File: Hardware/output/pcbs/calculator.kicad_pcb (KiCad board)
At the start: 4 copper layers, 70.5 x 143 mm, 46 parts

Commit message: feat: implement alpha key input support and unify error handling in RetroUIController
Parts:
- moved Disp 6.00 mm to (29.5, -125.9)
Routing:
- net P21: track 185.1 -> 51.6 mm, vias 3 -> 0
- net P20: track 89.1 -> 131.7 mm, vias 0 -> 3
- net P6: track 162.6 -> 197.1 mm, vias 4 -> 5
- net P1: track 134.6 -> 165.9 mm, vias 5 -> 4
- net P4: track 109.3 -> 132.8 mm, vias 6 -> 4
- net P10: track 173.3 -> 195.4 mm, vias 3 -> 4
- net P5: track 145.5 -> 167.1 mm, vias 3 -> 4
- net P14: track 135.2 -> 153.6 mm, vias 2 -> 1
- net P18: track 1.74 -> 19.9 mm
- net P16: track 86.2 -> 103.8 mm, vias 2 -> 1
- net GND: track 54.9 -> 67.0 mm, vias 1 -> 0
- net P0: track 129.8 -> 141.5 mm
- net P15: track 133.2 -> 142.1 mm, vias 2 -> 1
- net P9: track 141.7 -> 148.4 mm, vias 2 -> 1
- net P7: track 148.7 -> 155.3 mm, vias 2 -> 1
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- removed copper zone on In1.Cu, net GND
- removed copper zone on In2.Cu, net GND
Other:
- copper layers 4 -> 2

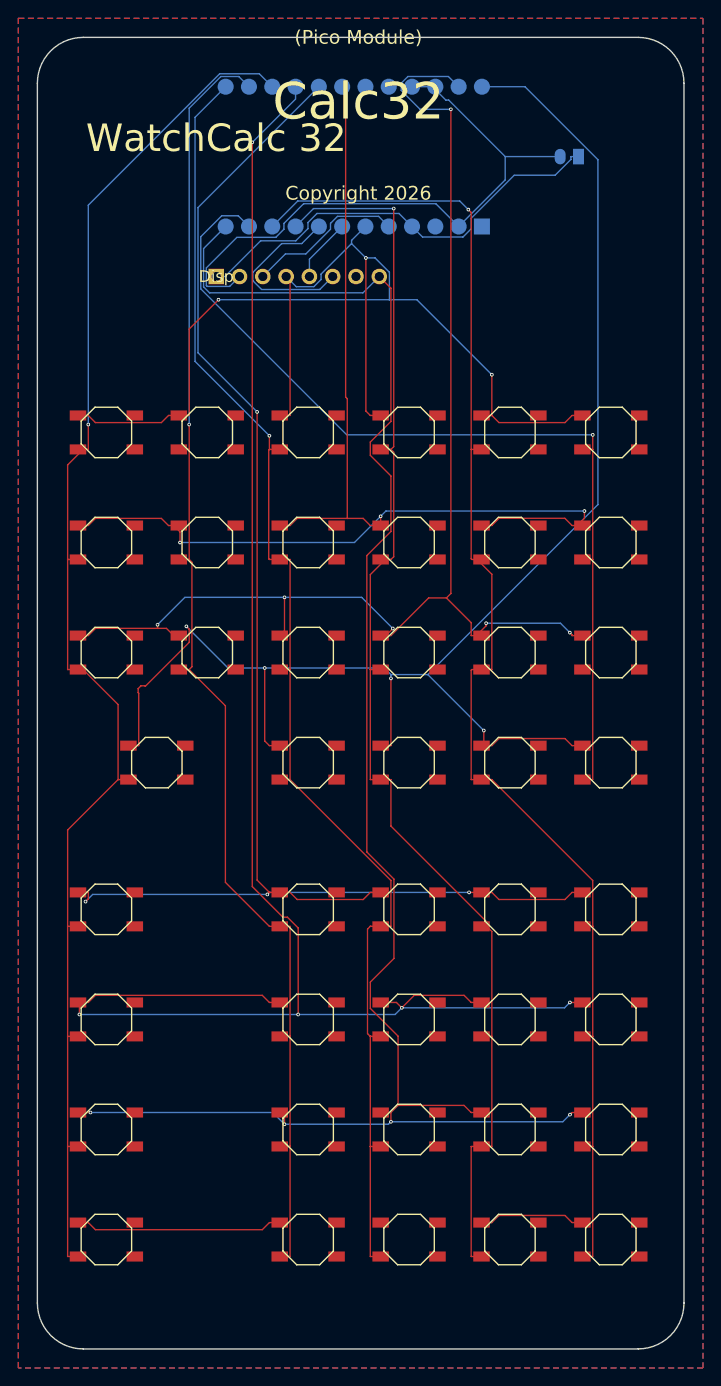
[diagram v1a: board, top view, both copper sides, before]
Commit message: fix: resolve display formatting bugs in hardware wrapper and streamline PCB manufacturing and ordering documentation.
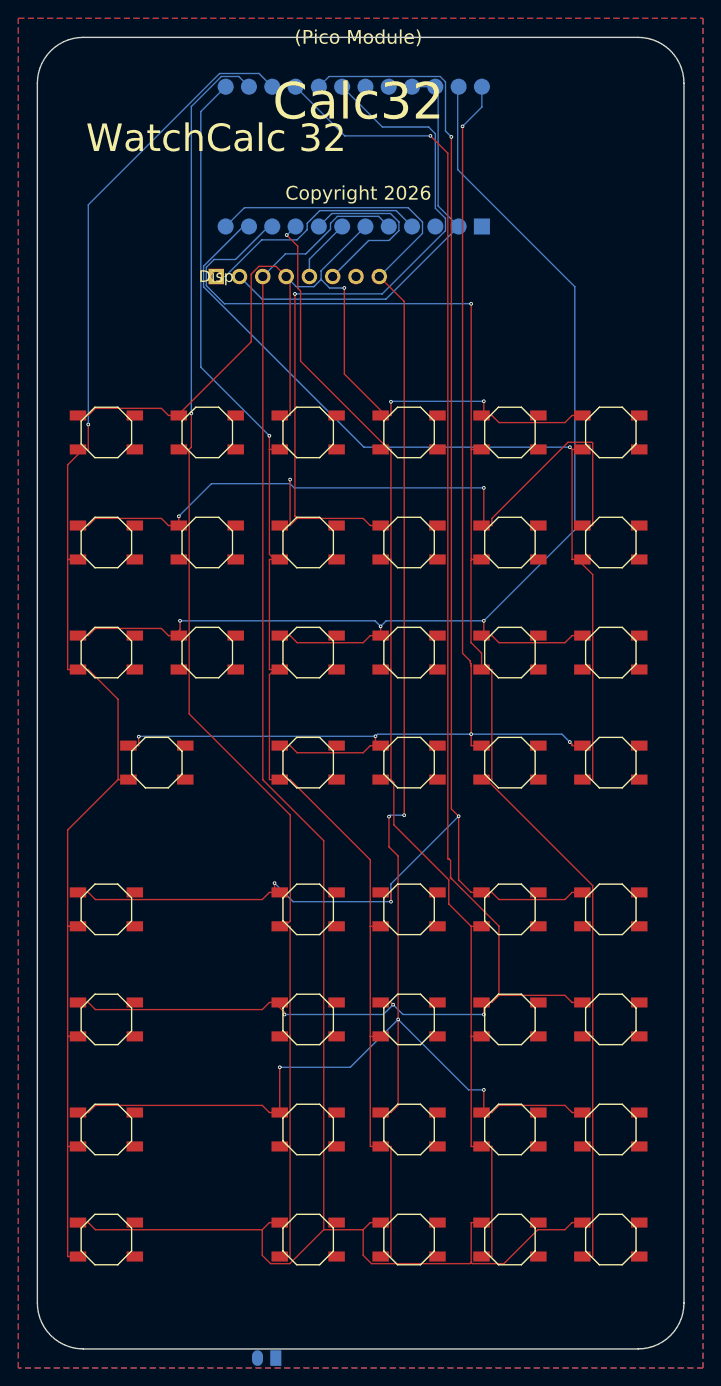
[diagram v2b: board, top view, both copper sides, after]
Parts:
- moved JST1 135.1 mm to (35.0, -8.00)
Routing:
- net P21: track 51.6 -> 199.0 mm
- net P4: track 132.8 -> 162.6 mm
- net P1: track 165.9 -> 138.1 mm, vias 4 -> 5
- net P20: track 131.7 -> 108.6 mm
- net VCC: track 48.4 -> 25.5 mm
- net P6: track 197.1 -> 175.4 mm, vias 5 -> 4
- net GND: track 67.0 -> 47.0 mm
- net P15: track 142.1 -> 131.0 mm
- net P16: track 103.8 -> 97.7 mm
- net P14: track 153.6 -> 158.9 mm
- net P5: track 167.1 -> 168.5 mm
- net P9: track 148.4 -> 147.1 mm
- net P0: track 141.5 -> 140.9 mm, vias 6 -> 3
- net P10: track 195.4 -> 195.9 mm, vias 4 -> 5

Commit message: feat: update PCB layout and chassis assets, and refine calculator engine logic
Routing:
- net P21: track 199.0 -> 614.0 mm, vias 0 -> 2
- net P6: track 175.4 -> 587.2 mm, vias 4 -> 13
- net P10: track 195.9 -> 599.6 mm, vias 5 -> 19
- net P8: track 146.4 -> 484.5 mm, vias 1 -> 3
- net P7: track 155.7 -> 463.0 mm, vias 1 -> 3
- net P5: track 168.5 -> 475.2 mm, vias 4 -> 13
- net P9: track 147.1 -> 451.6 mm, vias 1 -> 3
- net P15: track 131.0 -> 430.9 mm, vias 1 -> 3
- net P14: track 158.9 -> 454.9 mm, vias 1 -> 3
- net P0: track 140.9 -> 434.3 mm, vias 3 -> 10
- net P1: track 138.1 -> 409.5 mm, vias 5 -> 12
- net P4: track 162.6 -> 373.4 mm, vias 4 -> 12
- net P20: track 108.6 -> 300.7 mm
- net P16: track 97.7 -> 288.2 mm, vias 1 -> 3
- net GND: track 47.0 -> 147.3 mm
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- added copper zone on B.Cu, net (none)
- added copper zone on F.Cu, net (none)
- removed copper zone on B.Cu, net GND
- removed copper zone on F.Cu, net GND

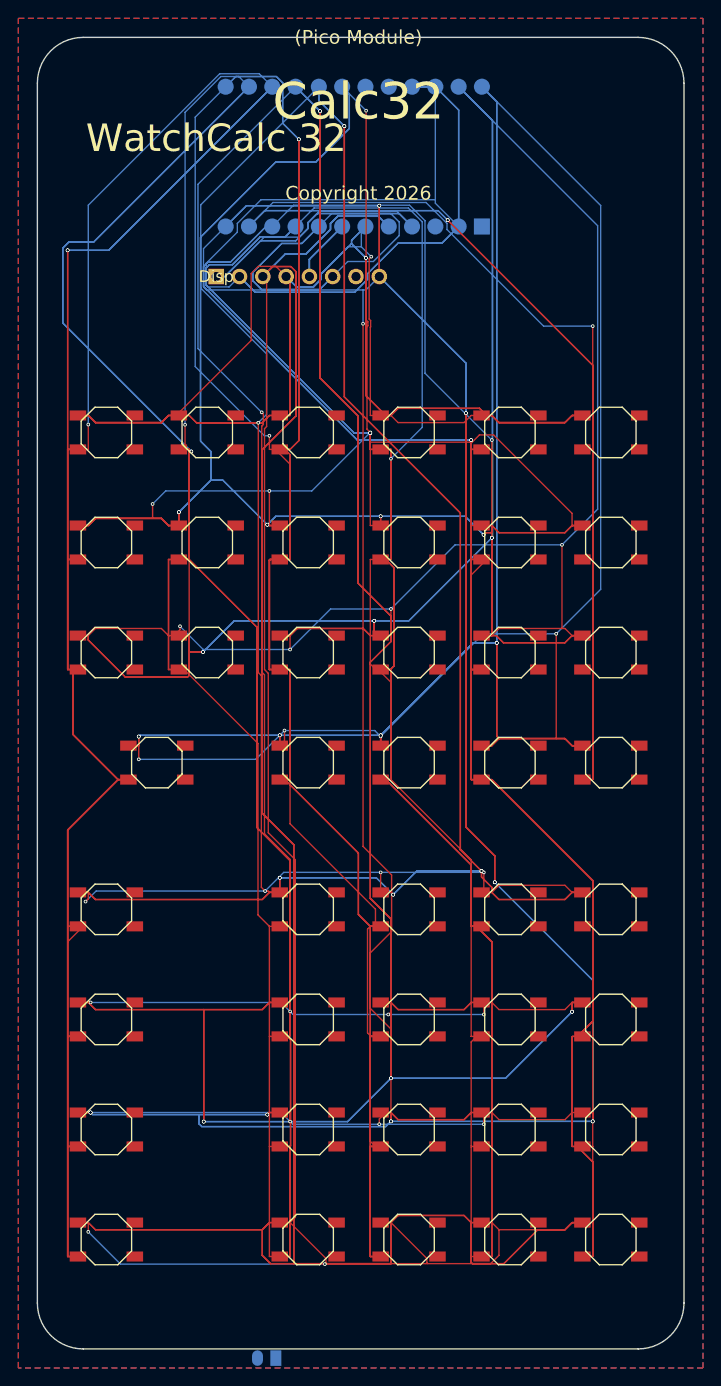
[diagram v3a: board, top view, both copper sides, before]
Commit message: refactor: update stack lift logic, add STL batching script, and adjust hardware geometry/routing
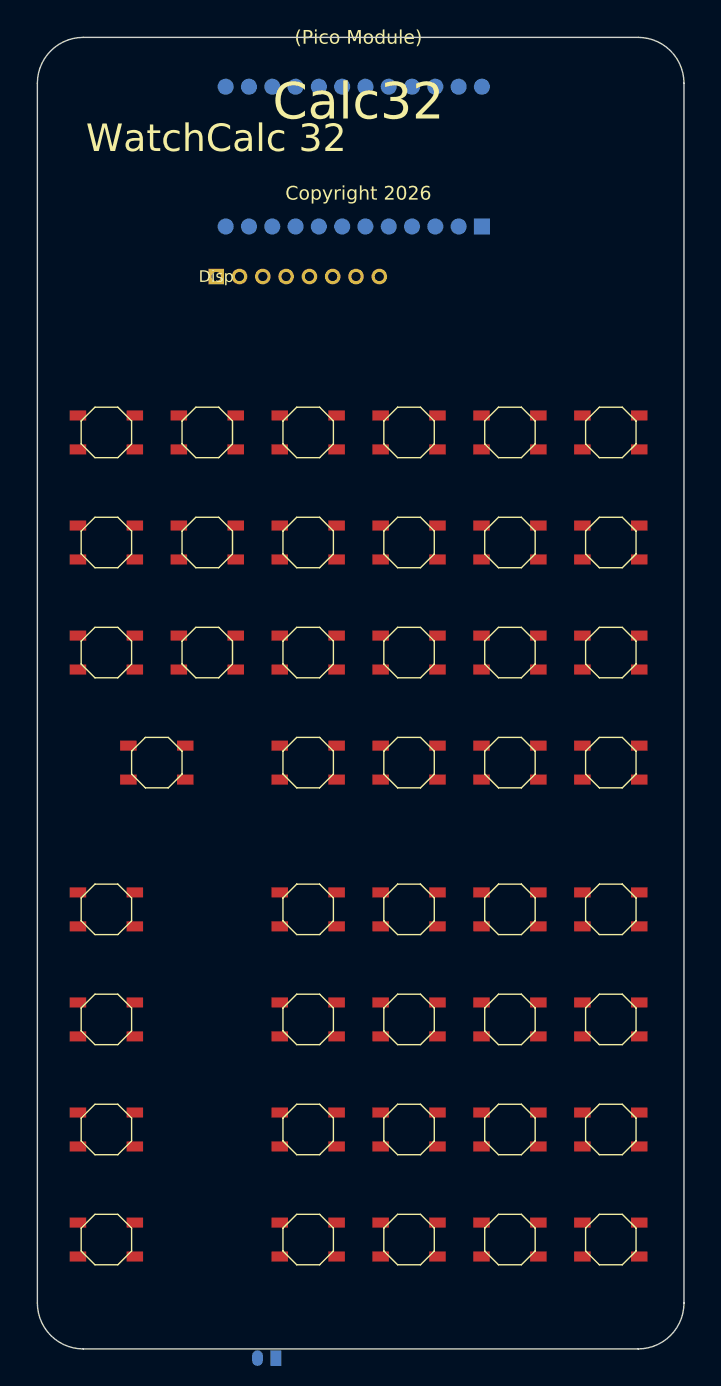
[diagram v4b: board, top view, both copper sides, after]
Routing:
- net P21: track 614.0 -> 0.00 mm, vias 2 -> 0
- net P10: track 599.6 -> 0.00 mm, vias 19 -> 0
- net P6: track 587.2 -> 0.00 mm, vias 13 -> 0
- net P8: track 484.5 -> 0.00 mm, vias 3 -> 0
- net P5: track 475.2 -> 0.00 mm, vias 13 -> 0
- net P7: track 463.0 -> 0.00 mm, vias 3 -> 0
- net P14: track 454.9 -> 0.00 mm, vias 3 -> 0
- net P9: track 451.6 -> 0.00 mm, vias 3 -> 0
- net P0: track 434.3 -> 0.00 mm, vias 10 -> 0
- net P15: track 430.9 -> 0.00 mm, vias 3 -> 0
- net P1: track 409.5 -> 0.00 mm, vias 12 -> 0
- net P4: track 373.4 -> 0.00 mm, vias 12 -> 0
- net P20: track 300.7 -> 0.00 mm, vias 3 -> 0
- net P16: track 288.2 -> 0.00 mm, vias 3 -> 0
- net GND: track 147.3 -> 0.00 mm
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- removed copper zone on B.Cu, net (none)
- removed copper zone on F.Cu, net (none)

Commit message: refactor: update hardware generation scripts for bezel geometry and modernize RPN core display logic and unicode mathematical operators.
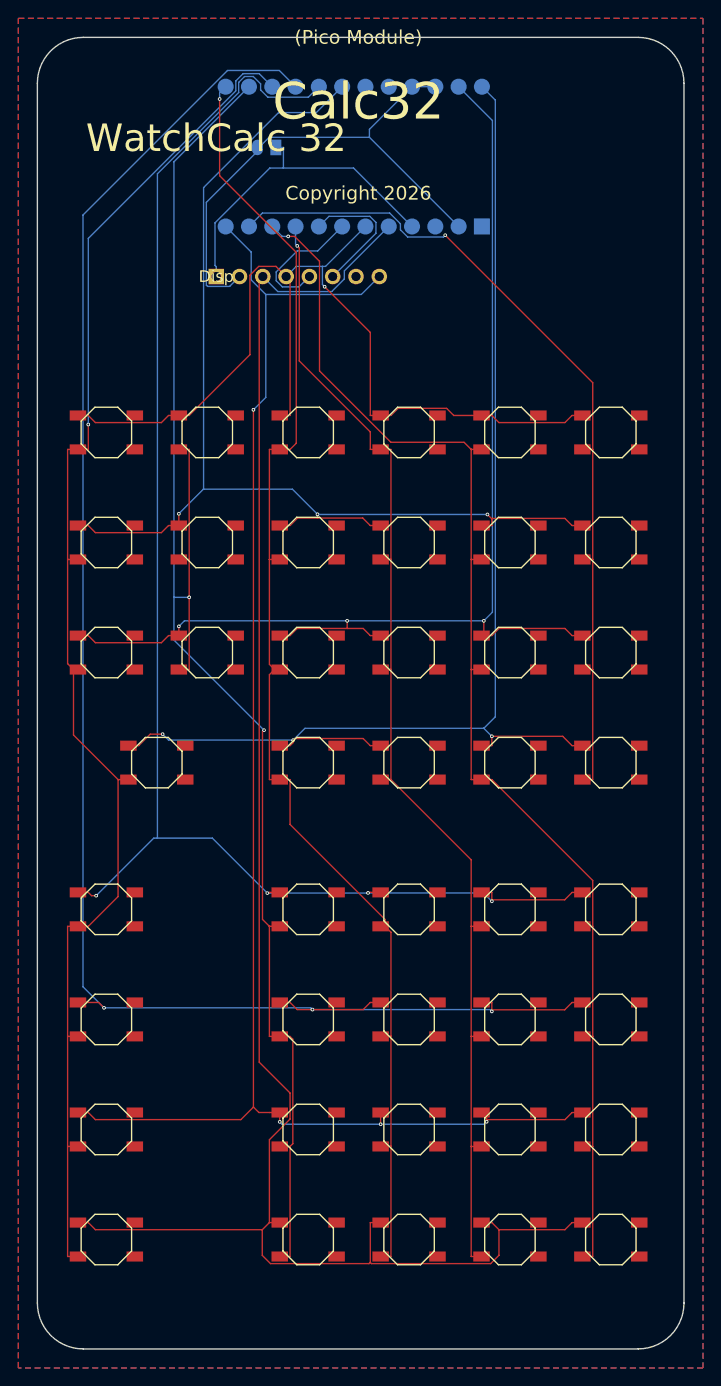
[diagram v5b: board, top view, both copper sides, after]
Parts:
- moved JST1 132.0 mm to (35.0, -140.0)
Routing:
- net P21: track 0.00 -> 195.5 mm
- net P6: track 0.00 -> 187.3 mm, vias 0 -> 3
- net P10: track 0.00 -> 172.1 mm, vias 0 -> 4
- net P8: track 0.00 -> 170.3 mm, vias 0 -> 2
- net P5: track 0.00 -> 162.7 mm, vias 0 -> 4
- net P7: track 0.00 -> 154.0 mm, vias 0 -> 1
- net P9: track 0.00 -> 146.6 mm, vias 0 -> 1
- net P14: track 0.00 -> 141.5 mm, vias 0 -> 1
- net P1: track 0.00 -> 136.6 mm, vias 0 -> 3
- net P0: track 0.00 -> 132.1 mm, vias 0 -> 3
- net P15: track 0.00 -> 129.4 mm, vias 0 -> 1
- net P4: track 0.00 -> 126.2 mm, vias 0 -> 3
- net P20: track 0.00 -> 105.8 mm, vias 0 -> 1
- net P16: track 0.00 -> 94.1 mm, vias 0 -> 1
- net GND: track 0.00 -> 58.2 mm
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- added copper zone on B.Cu, net GND
- added copper zone on F.Cu, net GND

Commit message: feat: replace E-Ink footprint with Sharp LCD connector and update calculator key map with new navigation actions
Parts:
- removed Disp: E-Ink, 
- added J1: Sharp_LCD, , F.Cu at (45.0, -130.0)
- moved JST1 132.0 mm to (35.0, -8.00)
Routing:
- net P21: track 195.5 -> 61.5 mm, vias 0 -> 1
- net P20: track 105.8 -> 152.9 mm, vias 1 -> 2
- net P4: track 126.2 -> 151.9 mm
- net GND: track 58.2 -> 32.7 mm, vias 0 -> 1
- net VCC: track 35.6 -> 10.4 mm, vias 0 -> 1
- net P8: track 170.3 -> 152.0 mm, vias 2 -> 1
- net P0: track 132.1 -> 144.4 mm, vias 3 -> 5
- net P1: track 136.6 -> 146.4 mm, vias 3 -> 4
- net P18: track 14.8 -> 5.69 mm, vias 0 -> 1
- net P6: track 187.3 -> 179.0 mm, vias 3 -> 4
- net P5: track 162.7 -> 169.7 mm, vias 4 -> 3
- net P16: track 94.1 -> 87.2 mm
- net P14: track 141.5 -> 136.7 mm
- net P19: track 14.6 -> 12.7 mm, vias 0 -> 1
- net P10: track 172.1 -> 173.7 mm
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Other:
- board text removed: "WatchCalc 32"

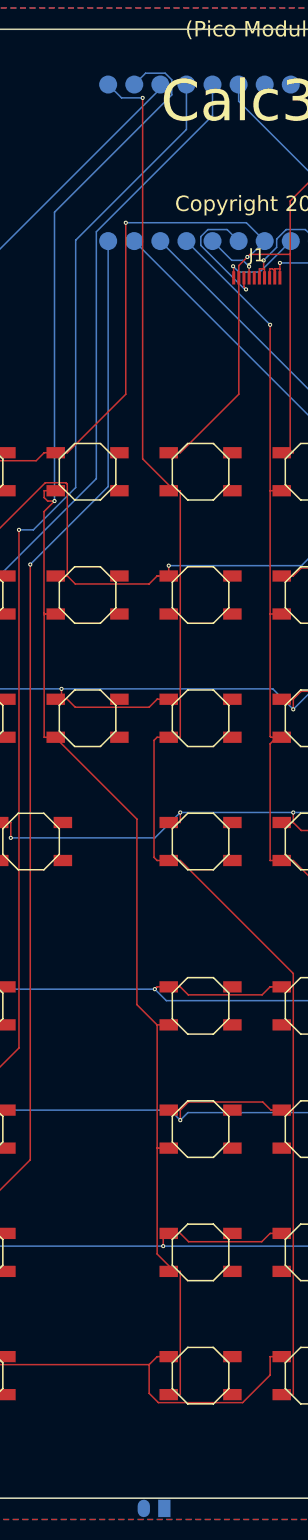
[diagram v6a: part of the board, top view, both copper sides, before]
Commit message: feat: upgrade display resolution to 400x240 and refactor UI layout engine for high-density rendering
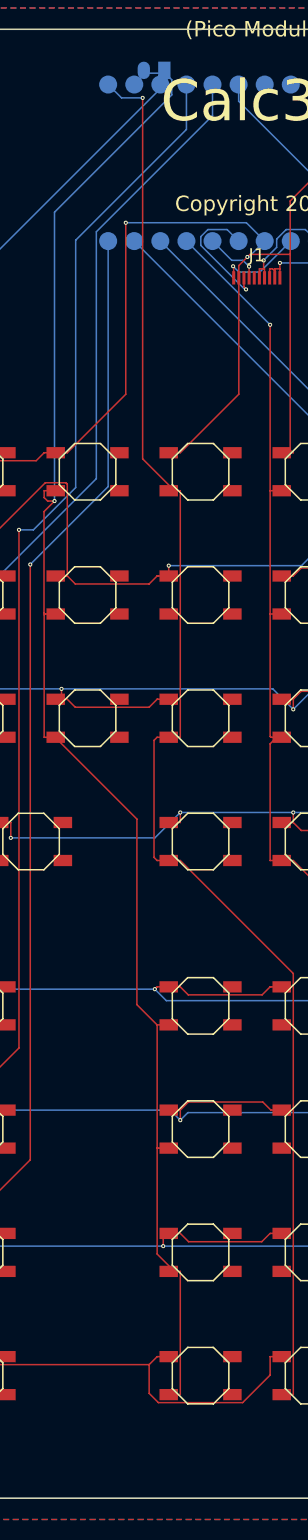
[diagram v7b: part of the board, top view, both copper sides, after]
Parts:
- moved JST1 140.0 mm to (35.0, -148.0)
